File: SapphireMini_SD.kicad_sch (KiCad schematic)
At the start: 11 parts, among them J301 503182-1852, U301 TPS22860DBVR, U302 MB85RS1MT

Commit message: Minor changes to annotation
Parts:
- renumbered R305 to R301, R301 to R302, R302 to R303, R303 to R304, R304 to R305, U302 to U301, U301 to U302
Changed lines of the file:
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@@
   (symbol (lib_id "power:GND") (at 226.06 123.19 0) (mirror y) (unit 1)
     (in_bom yes) (on_board yes)
-    (property "Reference" "#PWR0304" (id 0) (at 226.06 129.54 0)
+    (property "Reference" "#PWR0306" (id 0) (at 226.06 129.54 0)
       (effects (font (size 1.27 1.27)) hide)
     )
@@
   (symbol (lib_id "power:GND") (at 199.39 97.79 0) (unit 1)
     (in_bom yes) (on_board yes)
-    (property "Reference" "#PWR0303" (id 0) (at 199.39 104.14 0)
+    (property "Reference" "#PWR0304" (id 0) (at 199.39 104.14 0)
       (effects (font (size 1.27 1.27)) hide)
     )
@@
   (symbol (lib_id "Device:R_Small_US") (at 168.91 72.39 0) (unit 1)
     (in_bom yes) (on_board yes)
-    (property "Reference" "R302" (id 0) (at 170.6372 71.2216 0)
+    (property "Reference" "R303" (id 0) (at 170.6372 71.2216 0)
       (effects (font (size 1.27 1.27)) (justify left))
     )
@@
   (symbol (lib_id "Device:R_Small_US") (at 175.26 106.68 0) (unit 1)
     (in_bom yes) (on_board yes)
-    (property "Reference" "R303" (id 0) (at 176.9872 105.5116 0)
+    (property "Reference" "R304" (id 0) (at 176.9872 105.5116 0)
       (effects (font (size 1.27 1.27)) (justify left))
     )
@@
   (symbol (lib_id "Device:R_Small_US") (at 182.88 77.47 180) (unit 1)
     (in_bom yes) (on_board yes)
-    (property "Reference" "R304" (id 0) (at 184.6072 76.3016 0)
+    (property "Reference" "R305" (id 0) (at 184.6072 76.3016 0)
       (effects (font (size 1.27 1.27)) (justify right))
     )
@@
   (symbol (lib_id "power:GND") (at 144.78 110.49 0) (unit 1)
     (in_bom yes) (on_board yes)
-    (property "Reference" "#PWR0301" (id 0) (at 144.78 116.84 0)
+    (property "Reference" "#PWR0302" (id 0) (at 144.78 116.84 0)
       (effects (font (size 1.27 1.27)) hide)
     )
@@
   (symbol (lib_id "power:GND") (at 154.94 110.49 0) (unit 1)
     (in_bom yes) (on_board yes)
-    (property "Reference" "#PWR0302" (id 0) (at 154.94 116.84 0)
+    (property "Reference" "#PWR0303" (id 0) (at 154.94 116.84 0)
       (effects (font (size 1.27 1.27)) hide)
     )
@@
   (symbol (lib_id "Device:R_Small_US") (at 92.71 86.36 0) (unit 1)
     (in_bom yes) (on_board yes)
-    (property "Reference" "R301" (id 0) (at 86.36 83.82 0)
+    (property "Reference" "R302" (id 0) (at 86.36 83.82 0)
       (effects (font (size 1.27 1.27)) (justify left))
     )
@@
   (symbol (lib_id "sapphireMini:TPS22860DBVR") (at 121.92 101.6 0) (unit 1)
     (in_bom yes) (on_board yes)
-    (property "Reference" "U301" (id 0) (at 121.92 87.122 0))
+    (property "Reference" "U302" (id 0) (at 121.92 87.122 0))
     (property "Value" "TPS22860DBVR" (id 1) (at 121.92 89.4334 0))
     (property "Footprint" "SOT95P280X145-6N" (id 2) (at 121.92 101.6 0)
@@
   (symbol (lib_id "Device:R_Small_US") (at 71.12 142.24 180) (unit 1)
     (in_bom yes) (on_board yes)
-    (property "Reference" "R305" (id 0) (at 68.58 142.24 0)
+    (property "Reference" "R301" (id 0) (at 68.58 142.24 0)
       (effects (font (size 1.27 1.27)) (justify left))
     )
@@
   (symbol (lib_id "power:GND") (at 222.25 124.46 0) (mirror y) (unit 1)
     (in_bom yes) (on_board yes)
-    (property "Reference" "#PWR0306" (id 0) (at 222.25 130.81 0)
+    (property "Reference" "#PWR0305" (id 0) (at 222.25 130.81 0)
       (effects (font (size 1.27 1.27)) hide)
     )
@@
   (symbol (lib_id "power:GND") (at 102.87 157.48 0) (mirror y) (unit 1)
     (in_bom yes) (on_board yes)
-    (property "Reference" "#PWR0305" (id 0) (at 102.87 163.83 0)
+    (property "Reference" "#PWR0301" (id 0) (at 102.87 163.83 0)
       (effects (font (size 1.27 1.27)) hide)
     )
@@
   (symbol (lib_id "Device:R_Small_US") (at 227.33 104.14 90) (unit 1)
     (in_bom yes) (on_board yes)
-    (property "Reference" "R306" (id 0) (at 224.79 101.6 90)
+    (property "Reference" "R306" (id 0) (at 220.98 101.6 90)
       (effects (font (size 1.27 1.27)) (justify right))
     )
@@
   (symbol (lib_id "Memory_NVRAM:MB85RS1MT") (at 102.87 148.59 0) (unit 1)
     (in_bom yes) (on_board yes)
-    (property "Reference" "U302" (id 0) (at 105.41 142.24 0))
+    (property "Reference" "U301" (id 0) (at 105.41 142.24 0))
     (property "Value" "MB85RS1MT" (id 1) (at 95.25 142.24 0))
     (property "Footprint" "Package_SO:SOP-8_3.9x4.9mm_P1.27mm" (id 2) (at 93.98 149.86 0)

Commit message: daily update
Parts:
- added R307, R308, R309, R310: 47, Resistor_SMD:R_0603_1608Metric, symbol Device:R_US
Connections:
- net SPI_MOSI: now also R308.1, R309.1, R309.2; no longer U301.5 (SI)
- net SPI_SCK: now also R307.1, R310.1, R310.2; no longer U301.6 (SCK)
- new net: R308.2, U301.5 (SI)
- new net: R307.2, U301.6 (SCK)
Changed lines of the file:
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@@
   (junction (at 175.26 93.98) (diameter 0) (color 0 0 0 0)
   )
-  (wire (pts (xy 113.03 148.59) (xy 125.73 148.59))
-    (stroke (width 0) (type default) (color 0 0 0 0))
-  )
   (wire (pts (xy 99.06 93.98) (xy 97.79 92.71))
     (stroke (width 0) (type default) (color 0 0 0 0))
@@
     (stroke (width 0) (type default) (color 0 0 0 0))
   )
+  (wire (pts (xy 214.63 91.44) (xy 231.14 91.44))
+    (stroke (width 0) (type default) (color 0 0 0 0))
+  )
   (wire (pts (xy 71.12 147.32) (xy 71.12 144.78))
     (stroke (width 0) (type default) (color 0 0 0 0))
@@
     (stroke (width 0) (type default) (color 0 0 0 0))
   )
-  (wire (pts (xy 113.03 146.05) (xy 125.73 146.05))
-    (stroke (width 0) (type default) (color 0 0 0 0))
-  )
   (wire (pts (xy 220.98 121.92) (xy 220.98 107.95))
     (stroke (width 0) (type default) (color 0 0 0 0))
@@
     (stroke (width 0) (type default) (color 0 0 0 0))
   )
+  (wire (pts (xy 203.2 73.66) (xy 201.93 73.66))
+    (stroke (width 0) (type default) (color 0 0 0 0))
+  )
   (wire (pts (xy 231.14 111.76) (xy 227.33 111.76))
     (stroke (width 0) (type default) (color 0 0 0 0))
@@
     (stroke (width 0) (type default) (color 0 0 0 0))
   )
+  (wire (pts (xy 123.19 148.59) (xy 137.16 148.59))
+    (stroke (width 0) (type default) (color 0 0 0 0))
+  )
   (wire (pts (xy 170.18 60.96) (xy 168.91 62.23))
     (stroke (width 0) (type default) (color 0 0 0 0))
@@
     (stroke (width 0) (type default) (color 0 0 0 0))
   )
-  (wire (pts (xy 113.03 151.13) (xy 125.73 151.13))
+  (wire (pts (xy 113.03 151.13) (xy 137.16 151.13))
     (stroke (width 0) (type default) (color 0 0 0 0))
   )
@@
     (stroke (width 0) (type default) (color 0 0 0 0))
   )
+  (wire (pts (xy 113.03 148.59) (xy 115.57 148.59))
+    (stroke (width 0) (type default) (color 0 0 0 0))
+  )
   (wire (pts (xy 222.25 81.28) (xy 220.98 80.01))
     (stroke (width 0) (type default) (color 0 0 0 0))
@@
     (stroke (width 0) (type default) (color 0 0 0 0))
   )
-  (wire (pts (xy 213.36 73.66) (xy 201.93 73.66))
+  (wire (pts (xy 213.36 73.66) (xy 210.82 73.66))
     (stroke (width 0) (type default) (color 0 0 0 0))
   )
@@
     (stroke (width 0) (type default) (color 0 0 0 0))
   )
+  (wire (pts (xy 113.03 146.05) (xy 115.57 146.05))
+    (stroke (width 0) (type default) (color 0 0 0 0))
+  )
   (wire (pts (xy 218.44 99.06) (xy 217.17 100.33))
     (stroke (width 0) (type default) (color 0 0 0 0))
@@
     (stroke (width 0) (type default) (color 0 0 0 0))
   )
+  (wire (pts (xy 123.19 146.05) (xy 137.16 146.05))
+    (stroke (width 0) (type default) (color 0 0 0 0))
+  )
   (wire (pts (xy 182.88 67.31) (xy 182.88 74.93))
     (stroke (width 0) (type default) (color 0 0 0 0))
@@
     (stroke (width 0) (type default) (color 0 0 0 0))
   )
-  (wire (pts (xy 201.93 91.44) (xy 231.14 91.44))
+  (wire (pts (xy 201.93 91.44) (xy 207.01 91.44))
     (stroke (width 0) (type default) (color 0 0 0 0))
   )
@@
     (effects (font (size 1.27 1.27)) (justify left bottom))
   )
-  (label "SPI_MOSI" (at 115.57 148.59 0)
+  (label "SPI_MOSI" (at 127 148.59 0)
     (effects (font (size 1.27 1.27)) (justify left bottom))
   )
@@
     (effects (font (size 1.27 1.27)) (justify left bottom))
   )
-  (label "SPI_SCK" (at 115.57 146.05 0)
-    (effects (font (size 1.27 1.27)) (justify left bottom))
-  )
-  (label "SPI_MISO" (at 115.57 151.13 0)
+  (label "SPI_SCK" (at 127 146.05 0)
+    (effects (font (size 1.27 1.27)) (justify left bottom))
+  )
+  (label "SPI_MISO" (at 127 151.13 0)
     (effects (font (size 1.27 1.27)) (justify left bottom))
   )
@@
     (pin "6")
   )
+  (symbol (lib_id "Device:R_US") (at 207.01 73.66 270) (unit 1)
+    (in_bom yes) (on_board yes)
+    (property "Reference" "R309" (id 0) (at 203.2 72.39 90))
+    (property "Value" "47" (id 1) (at 209.55 72.39 90))
+    (property "Footprint" "Resistor_SMD:R_0603_1608Metric" (id 2) (at 206.756 74.676 90)
+      (effects (font (size 1.27 1.27)) hide)
+    )
+    (property "Datasheet" "~" (id 3) (at 207.01 73.66 0)
+      (effects (font (size 1.27 1.27)) hide)
+    )
+    (pin "1")
+    (pin "2")
+  )
   (symbol (lib_id "Device:R_Small_US") (at 71.12 142.24 180) (unit 1)
     (in_bom yes) (on_board yes)
@@
     )
     (pin "1")
+  )
+  (symbol (lib_id "Device:R_US") (at 119.38 148.59 270) (unit 1)
+    (in_bom yes) (on_board yes)
+    (property "Reference" "R308" (id 0) (at 115.57 147.32 90))
+    (property "Value" "47" (id 1) (at 121.92 147.32 90))
+    (property "Footprint" "Resistor_SMD:R_0603_1608Metric" (id 2) (at 119.126 149.606 90)
+      (effects (font (size 1.27 1.27)) hide)
+    )
+    (property "Datasheet" "~" (id 3) (at 119.38 148.59 0)
+      (effects (font (size 1.27 1.27)) hide)
+    )
+    (pin "1")
+    (pin "2")
+  )
+  (symbol (lib_id "Device:R_US") (at 210.82 91.44 270) (unit 1)
+    (in_bom yes) (on_board yes)
+    (property "Reference" "R310" (id 0) (at 207.01 90.17 90))
+    (property "Value" "47" (id 1) (at 213.36 90.17 90))
+    (property "Footprint" "Resistor_SMD:R_0603_1608Metric" (id 2) (at 210.566 92.456 90)
+      (effects (font (size 1.27 1.27)) hide)
+    )
+    (property "Datasheet" "~" (id 3) (at 210.82 91.44 0)
+      (effects (font (size 1.27 1.27)) hide)
+    )
+    (pin "1")
+    (pin "2")
   )
   (symbol (lib_id "503182-1852:503182-1852") (at 236.22 96.52 0) (unit 1)
@@
     (pin "SW")
   )
+  (symbol (lib_id "Device:R_US") (at 119.38 146.05 270) (unit 1)
+    (in_bom yes) (on_board yes)
+    (property "Reference" "R307" (id 0) (at 115.57 144.78 90))
+    (property "Value" "47" (id 1) (at 121.92 144.78 90))
+    (property "Footprint" "Resistor_SMD:R_0603_1608Metric" (id 2) (at 119.126 147.066 90)
+      (effects (font (size 1.27 1.27)) hide)
+    )
+    (property "Datasheet" "~" (id 3) (at 119.38 146.05 0)
+      (effects (font (size 1.27 1.27)) hide)
+    )
+    (pin "1")
+    (pin "2")
+  )
   (symbol (lib_id "Device:R_Small_US") (at 227.33 104.14 90) (unit 1)

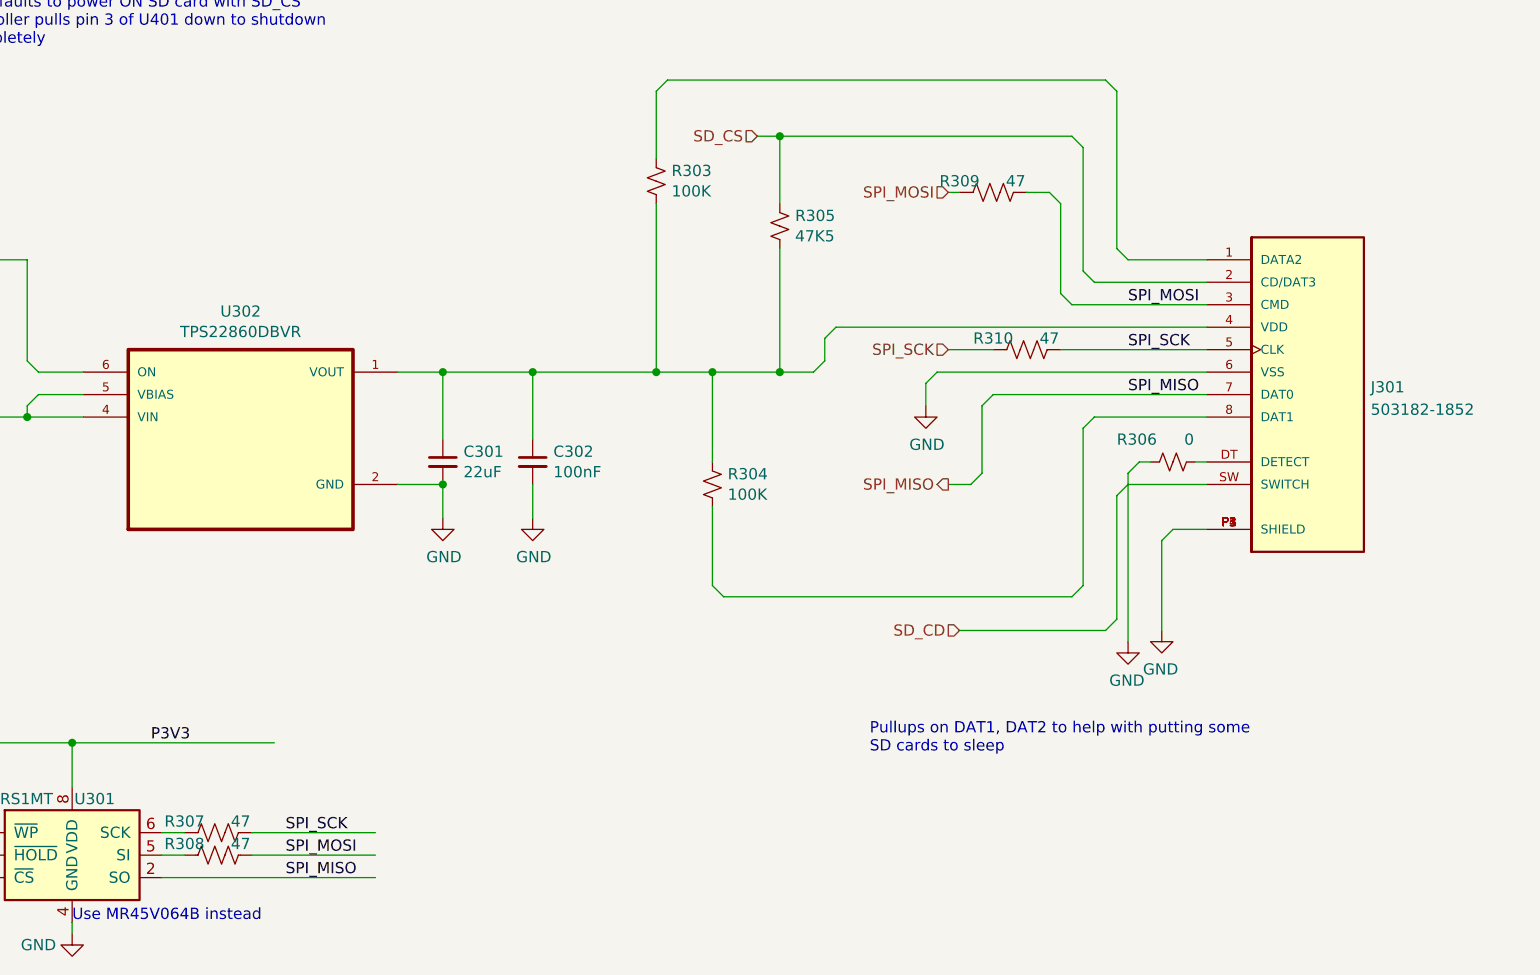
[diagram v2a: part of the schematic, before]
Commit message: Footprints complete. Starting layout
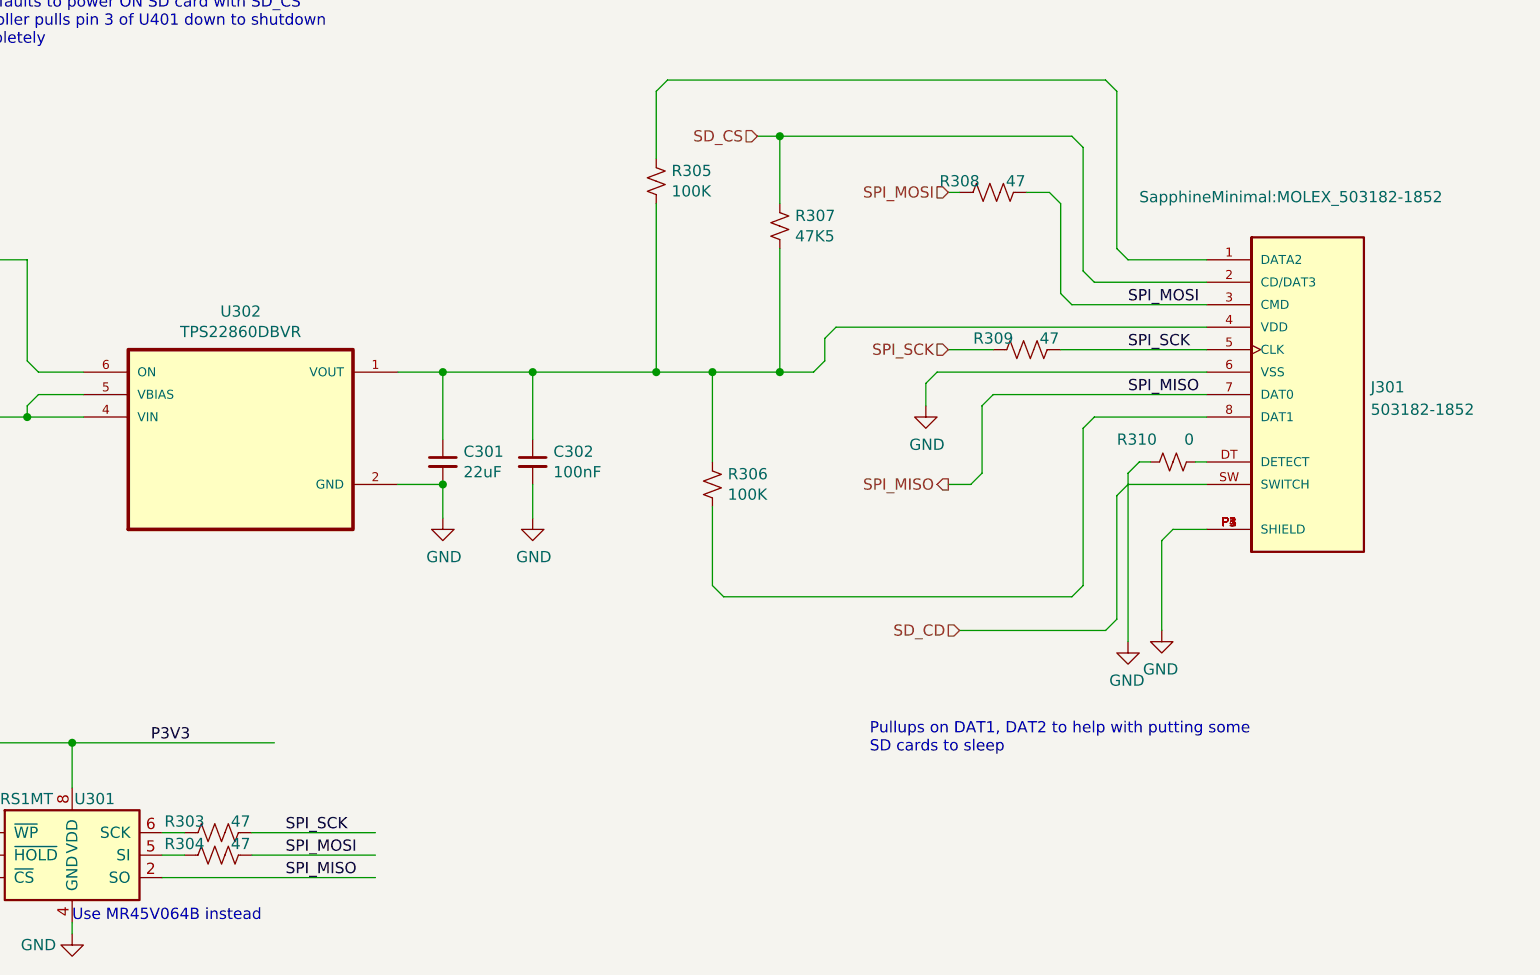
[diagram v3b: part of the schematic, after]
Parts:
- C301: MPN CGA5L1X5R1C226M160AC -> CL21A226MAYNNNE; Manufacturer TDK -> Samsung
- C302: MPN CL10B104KA8NNNC -> CL05A104KA5NNNC
- J301: footprint MOLEX_503182-1852 -> SapphineMinimal:MOLEX_503182-1852; MPN (none) -> 503182-1852; Manufacturer (none) -> Amphenol ICC (FCI)
- renumbered R307 to R303, R308 to R304, R303 to R305, R304 to R306, R305 to R307, R309 to R308, R310 to R309, R306 to R310
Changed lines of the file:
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@@
   (symbol (lib_id "Device:R_Small_US") (at 168.91 72.39 0) (unit 1)
     (in_bom yes) (on_board yes)
-    (property "Reference" "R303" (id 0) (at 170.6372 71.2216 0)
+    (property "Reference" "R305" (id 0) (at 170.6372 71.2216 0)
       (effects (font (size 1.27 1.27)) (justify left))
     )
@@
   (symbol (lib_id "Device:R_Small_US") (at 175.26 106.68 0) (unit 1)
     (in_bom yes) (on_board yes)
-    (property "Reference" "R304" (id 0) (at 176.9872 105.5116 0)
+    (property "Reference" "R306" (id 0) (at 176.9872 105.5116 0)
       (effects (font (size 1.27 1.27)) (justify left))
     )
@@
       (effects (font (size 1.27 1.27)) hide)
     )
-    (property "MPN" "CL10B104KA8NNNC" (id 5) (at 154.94 104.14 0)
+    (property "MPN" "CL05A104KA5NNNC" (id 5) (at 154.94 104.14 0)
       (effects (font (size 1.27 1.27)) hide)
     )
@@
       (effects (font (size 1.27 1.27)) hide)
     )
-    (property "Description" "0.1 µF ±10% 25V Ceramic Capacitor X7R 0603 (1608 Metric)" (id 15) (at 154.94 104.14 0)
+    (property "Description" "0.1 µF ±10% 25V Ceramic Capacitor X5R 0402 (1005 Metric)" (id 15) (at 154.94 104.14 0)
       (effects (font (size 1.27 1.27)) hide)
     )
@@
   (symbol (lib_id "Device:R_Small_US") (at 182.88 77.47 180) (unit 1)
     (in_bom yes) (on_board yes)
-    (property "Reference" "R305" (id 0) (at 184.6072 76.3016 0)
+    (property "Reference" "R307" (id 0) (at 184.6072 76.3016 0)
       (effects (font (size 1.27 1.27)) (justify right))
     )
@@
       (effects (font (size 1.27 1.27)) hide)
     )
-    (property "MPN" "CGA5L1X5R1C226M160AC" (id 5) (at 144.78 104.14 0)
-      (effects (font (size 1.27 1.27)) hide)
-    )
-    (property "Manufacturer" "TDK" (id 6) (at 144.78 104.14 0)
+    (property "MPN" "CL21A226MAYNNNE" (id 5) (at 144.78 104.14 0)
+      (effects (font (size 1.27 1.27)) hide)
+    )
+    (property "Manufacturer" "Samsung" (id 6) (at 144.78 104.14 0)
       (effects (font (size 1.27 1.27)) hide)
     )
@@
       (effects (font (size 1.27 1.27)) hide)
     )
-    (property "Description" "22 µF ±20% 16V Ceramic Capacitor X5R 1206" (id 15) (at 144.78 104.14 0)
+    (property "Description" "22 µF ±20% 25V Ceramic Capacitor X5R 0805 (2012 Metric)" (id 15) (at 144.78 104.14 0)
       (effects (font (size 1.27 1.27)) hide)
     )
@@
   (symbol (lib_id "Device:R_US") (at 207.01 73.66 270) (unit 1)
     (in_bom yes) (on_board yes)
-    (property "Reference" "R309" (id 0) (at 203.2 72.39 90))
+    (property "Reference" "R308" (id 0) (at 203.2 72.39 90))
     (property "Value" "47" (id 1) (at 209.55 72.39 90))
     (property "Footprint" "Resistor_SMD:R_0603_1608Metric" (id 2) (at 206.756 74.676 90)
@@
   (symbol (lib_id "Device:R_US") (at 119.38 148.59 270) (unit 1)
     (in_bom yes) (on_board yes)
-    (property "Reference" "R308" (id 0) (at 115.57 147.32 90))
+    (property "Reference" "R304" (id 0) (at 115.57 147.32 90))
     (property "Value" "47" (id 1) (at 121.92 147.32 90))
     (property "Footprint" "Resistor_SMD:R_0603_1608Metric" (id 2) (at 119.126 149.606 90)
@@
   (symbol (lib_id "Device:R_US") (at 210.82 91.44 270) (unit 1)
     (in_bom yes) (on_board yes)
-    (property "Reference" "R310" (id 0) (at 207.01 90.17 90))
+    (property "Reference" "R309" (id 0) (at 207.01 90.17 90))
     (property "Value" "47" (id 1) (at 213.36 90.17 90))
     (property "Footprint" "Resistor_SMD:R_0603_1608Metric" (id 2) (at 210.566 92.456 90)
@@
   )
   (symbol (lib_id "503182-1852:503182-1852") (at 236.22 96.52 0) (unit 1)
-    (in_bom yes) (on_board yes) (fields_autoplaced)
+    (in_bom yes) (on_board yes)
     (property "Reference" "J301" (id 0) (at 249.682 95.6853 0)
       (effects (font (size 1.27 1.27)) (justify left))
@@
       (effects (font (size 1.27 1.27)) (justify left))
     )
-    (property "Footprint" "MOLEX_503182-1852" (id 2) (at 236.22 96.52 0)
-      (effects (font (size 1.27 1.27)) (justify left bottom) hide)
+    (property "Footprint" "SapphineMinimal:MOLEX_503182-1852" (id 2) (at 223.52 74.93 0)
+      (effects (font (size 1.27 1.27)) (justify left bottom))
     )
     (property "Datasheet" "" (id 3) (at 236.22 96.52 0)
@@
     (property "MANUFACTURER" "Molex" (id 4) (at 236.22 96.52 0)
       (effects (font (size 1.27 1.27)) (justify left bottom) hide)
+    )
+    (property "Description" "MICRO SD NORMAL ULTRALOWPRO8CKTE" (id 5) (at 236.22 96.52 0)
+      (effects (font (size 1.27 1.27)) hide)
+    )
+    (property "MPN" "503182-1852" (id 6) (at 236.22 96.52 0)
+      (effects (font (size 1.27 1.27)) hide)
+    )
+    (property "Manufacturer" "Amphenol ICC (FCI)" (id 7) (at 236.22 96.52 0)
+      (effects (font (size 1.27 1.27)) hide)
     )
     (pin "1")
@@
   (symbol (lib_id "Device:R_US") (at 119.38 146.05 270) (unit 1)
     (in_bom yes) (on_board yes)
-    (property "Reference" "R307" (id 0) (at 115.57 144.78 90))
+    (property "Reference" "R303" (id 0) (at 115.57 144.78 90))
     (property "Value" "47" (id 1) (at 121.92 144.78 90))
     (property "Footprint" "Resistor_SMD:R_0603_1608Metric" (id 2) (at 119.126 147.066 90)
@@
   (symbol (lib_id "Device:R_Small_US") (at 227.33 104.14 90) (unit 1)
     (in_bom yes) (on_board yes)
-    (property "Reference" "R306" (id 0) (at 220.98 101.6 90)
+    (property "Reference" "R310" (id 0) (at 220.98 101.6 90)
       (effects (font (size 1.27 1.27)) (justify right))
     )
